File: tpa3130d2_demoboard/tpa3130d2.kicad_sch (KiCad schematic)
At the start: 10 parts, among them J4 Barrel_Jack_MountingPin, U1 TPA3130D2DAPR

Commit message: Scheme complete
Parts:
- added C207: 1uF, symbol Device:C
- added R200: DNP, symbol Device:R
- added R201: 5kR6, symbol Device:R
- added R202, R203: 47kR, symbol Device:R
- renumbered C1 to C200, C2 to C201, C3 to C202, C4 to C203, C5 to C204, C6 to C205, C7 to C206, D1 to D200, J4 to J200
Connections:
- net +15V: now also R202.1
- net GND: now also U1.1 (MODSEL), U1.13 (AM2), U1.14 (AM1), U1.15 (AM0), C207.2, R201.2, R203.2
- net MUTE: now reaches U1.12 (MUTE)
- net MUTE: now also R203.1
- net at U1.2 (SDZ): now also U1.3 (FAULTZ), R202.2
- net at U1.6 (PLIMIT): now also U1.7 (GVDD), C207.1, R200.1
- net at U1.8 (GAIN_SLV): now also R200.2, R201.1
- no-connect marks 0 -> 1
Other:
- note added: "PLIM=GVDD-> No power limit Master, Gain=20dB, Rin=60k"

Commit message: Fill BOM
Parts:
- removed C207: 1uF, symbol Device:C
- added C207: 1uF, Capacitor_Tantalum_SMD:CP_EIA-3216-18_Kemet-A, symbol Device:C_Polarized
- C200, C201: footprint (none) -> Capacitor_THT:CP_Radial_D6.3mm_P2.50mm; Manufacturer (none) -> Rubycon; Part Number (none) -> 25YXJ220M6.3X11
- C202, C203, C204, C205, C206: footprint (none) -> Capacitor_SMD:C_0603_1608Metric; Manufacturer (none) -> Samsung Electro-Mechanics; Part Number (none) -> CL10B224KA8NNNC
- D200: footprint (none) -> Diode_SMD:D_PowerDI-123; Manufacturer (none) -> Diodes Incorporated; Part Number (none) -> SBR3M30P1-7
- J200: Manufacturer (none) -> XUNPU; Part Number (none) -> DC-005-A200
- R200: footprint (none) -> Resistor_SMD:R_0603_1608Metric; now not fitted
- R201: footprint (none) -> Resistor_SMD:R_0603_1608Metric; Manufacturer (none) -> UNI-ROYAL(Uniroyal Elec); Part Number (none) -> 0603WAF5601T5E
- R202, R203: footprint (none) -> Resistor_SMD:R_0603_1608Metric; Manufacturer (none) -> UNI-ROYAL(Uniroyal Elec); Part Number (none) -> 0603WAJ0473T5E
- U200: renamed from U1; Manufacturer (none) -> Texas Instruments; Part Number (none) -> TPA3130D2DAPR
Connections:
- net GND: now also C207.2
- net at R200.1, U200.6 (PLIMIT), U200.7 (GVDD): now also C207.1

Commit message: Initial PCB layout
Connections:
- net +15V: now also U200.17 (AVCC), U200.18 (PVCC), U200.19 (PVCC), U200.31 (PVCC), U200.32 (PVCC)
- net GND: no longer U200.17 (AVCC), U200.18 (PVCC), U200.19 (PVCC), U200.31 (PVCC), U200.32 (PVCC)
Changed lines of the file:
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@@
+	)
+	(junction
+		(at 166.37 25.4)
+		(diameter 0)
+		(color 0 0 0 0)
 	)
 	(junction
@@
 	)
 	(junction
-		(at 166.37 39.37)
-		(diameter 0)
-		(color 0 0 0 0)
-	)
-	(junction
 		(at 144.78 127)
 		(diameter 0)
@@
 	(junction
 		(at 76.2 39.37)
+		(diameter 0)
+		(color 0 0 0 0)
+	)
+	(junction
+		(at 176.53 54.61)
 		(diameter 0)
 		(color 0 0 0 0)
@@
 	(wire
 		(pts
+			(xy 176.53 54.61) (xy 179.07 54.61)
+		)
+		(stroke
+			(width 0)
+			(type default)
+		)
+	)
+	(wire
+		(pts
 			(xy 127 109.22) (xy 107.95 109.22)
 		)
@@
 	(wire
 		(pts
+			(xy 166.37 25.4) (xy 179.07 25.4)
+		)
+		(stroke
+			(width 0)
+			(type default)
+		)
+	)
+	(wire
+		(pts
 			(xy 102.87 25.4) (xy 115.57 25.4)
 		)
@@
 	(wire
 		(pts
-			(xy 168.91 39.37) (xy 166.37 39.37)
-		)
-		(stroke
-			(width 0)
-			(type default)
-		)
-	)
-	(wire
-		(pts
 			(xy 140.97 39.37) (xy 140.97 36.83)
 		)
@@
 	(wire
 		(pts
-			(xy 168.91 39.37) (xy 168.91 54.61)
-		)
-		(stroke
-			(width 0)
-			(type default)
-		)
-	)
-	(wire
-		(pts
 			(xy 139.7 81.28) (xy 147.32 81.28)
 		)
@@
 		(pts
 			(xy 90.17 39.37) (xy 102.87 39.37)
+		)
+		(stroke
+			(width 0)
+			(type default)
+		)
+	)
+	(wire
+		(pts
+			(xy 179.07 25.4) (xy 179.07 54.61)
 		)
 		(stroke
@@
 	(label "MUTE"
 		(at 140.97 119.38 0)
-		(fields_autoplaced yes)
 		(effects
 			(font

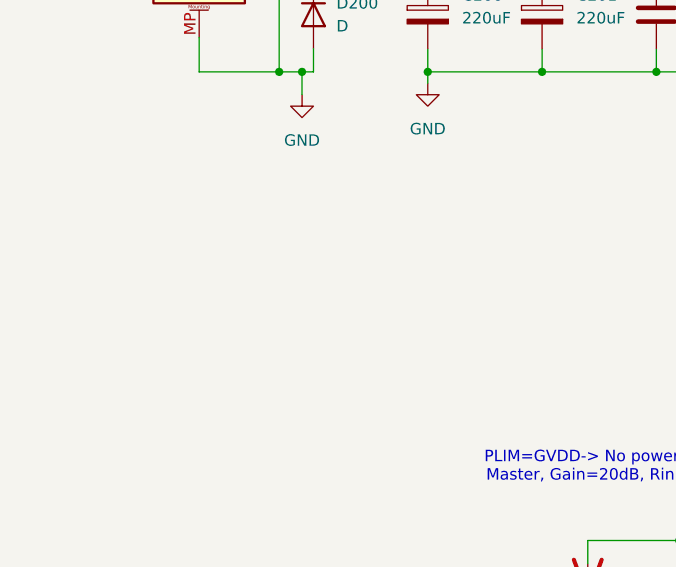
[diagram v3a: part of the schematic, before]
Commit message: Minor changes in terminal block footprint
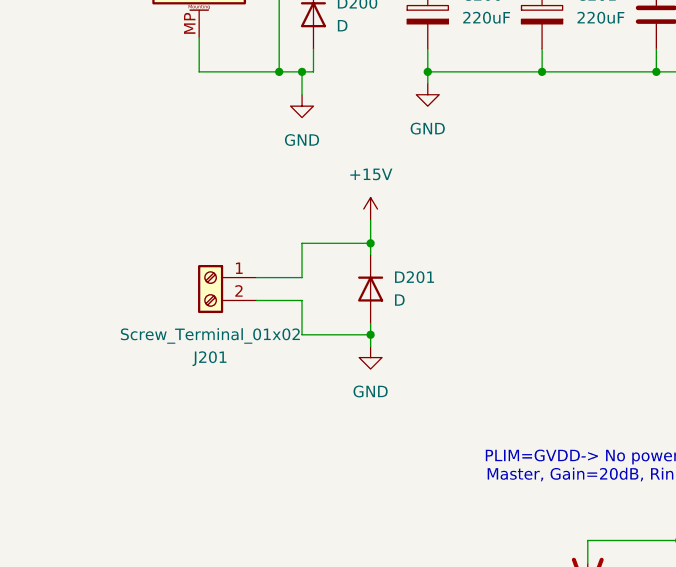
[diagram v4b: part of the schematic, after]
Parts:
- added D201: D, Diode_SMD:D_PowerDI-123, symbol Device:D
- added J201: Screw_Terminal_01x02, tpa3130d2_demoboard:terminal_block, symbol Connector:Screw_Terminal_01x02
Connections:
- net +15V: now also D201.1 (K), J201.1 (Pin_1)
- net GND: now also D201.2 (A), J201.2 (Pin_2)
